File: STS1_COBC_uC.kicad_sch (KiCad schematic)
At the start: 42 parts, among them IC2 STWD100PYW83F, IC3 STM32F411RET6TR, J11 Conn_01x01_Male, J12 Conn_01x01_Male, J13 Conn_01x01_Male, J14 Conn_01x01_Male, J15 Conn_01x01_Male, J16 Conn_ARM_JTAG_SWD_10, J17 Conn_01x03_Male, J18 Conn_01x01_Male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

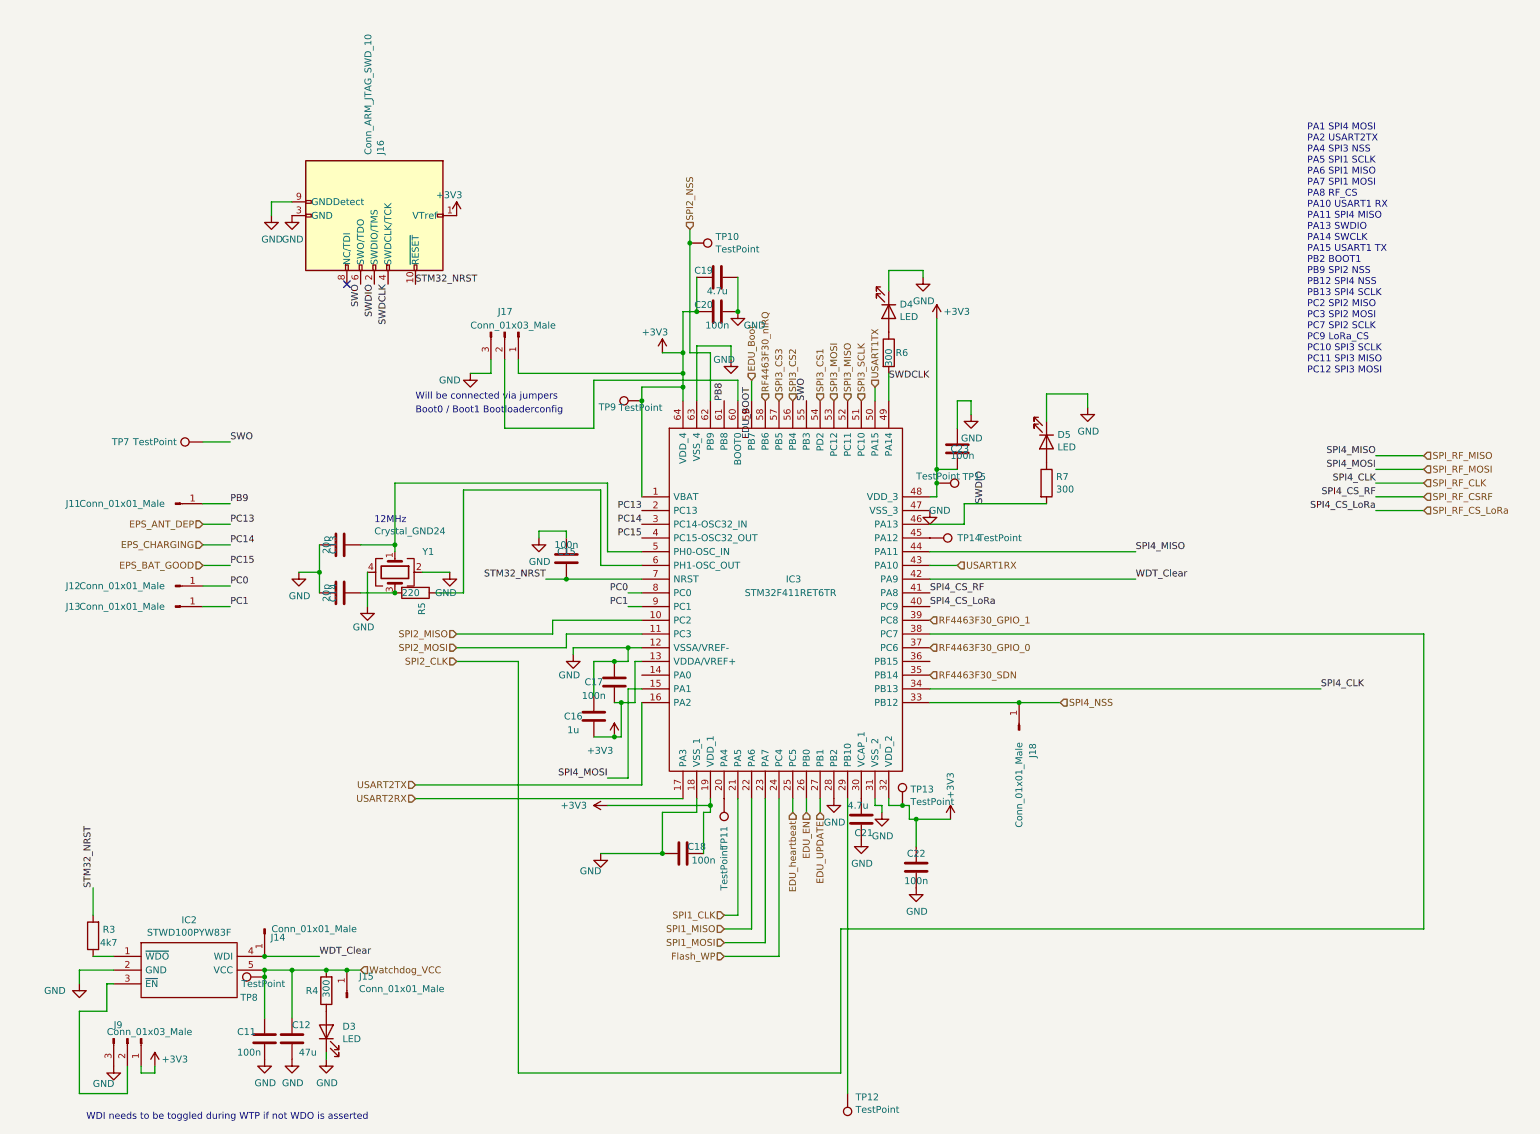
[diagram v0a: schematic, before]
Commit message: more work done
All parts besides RF added
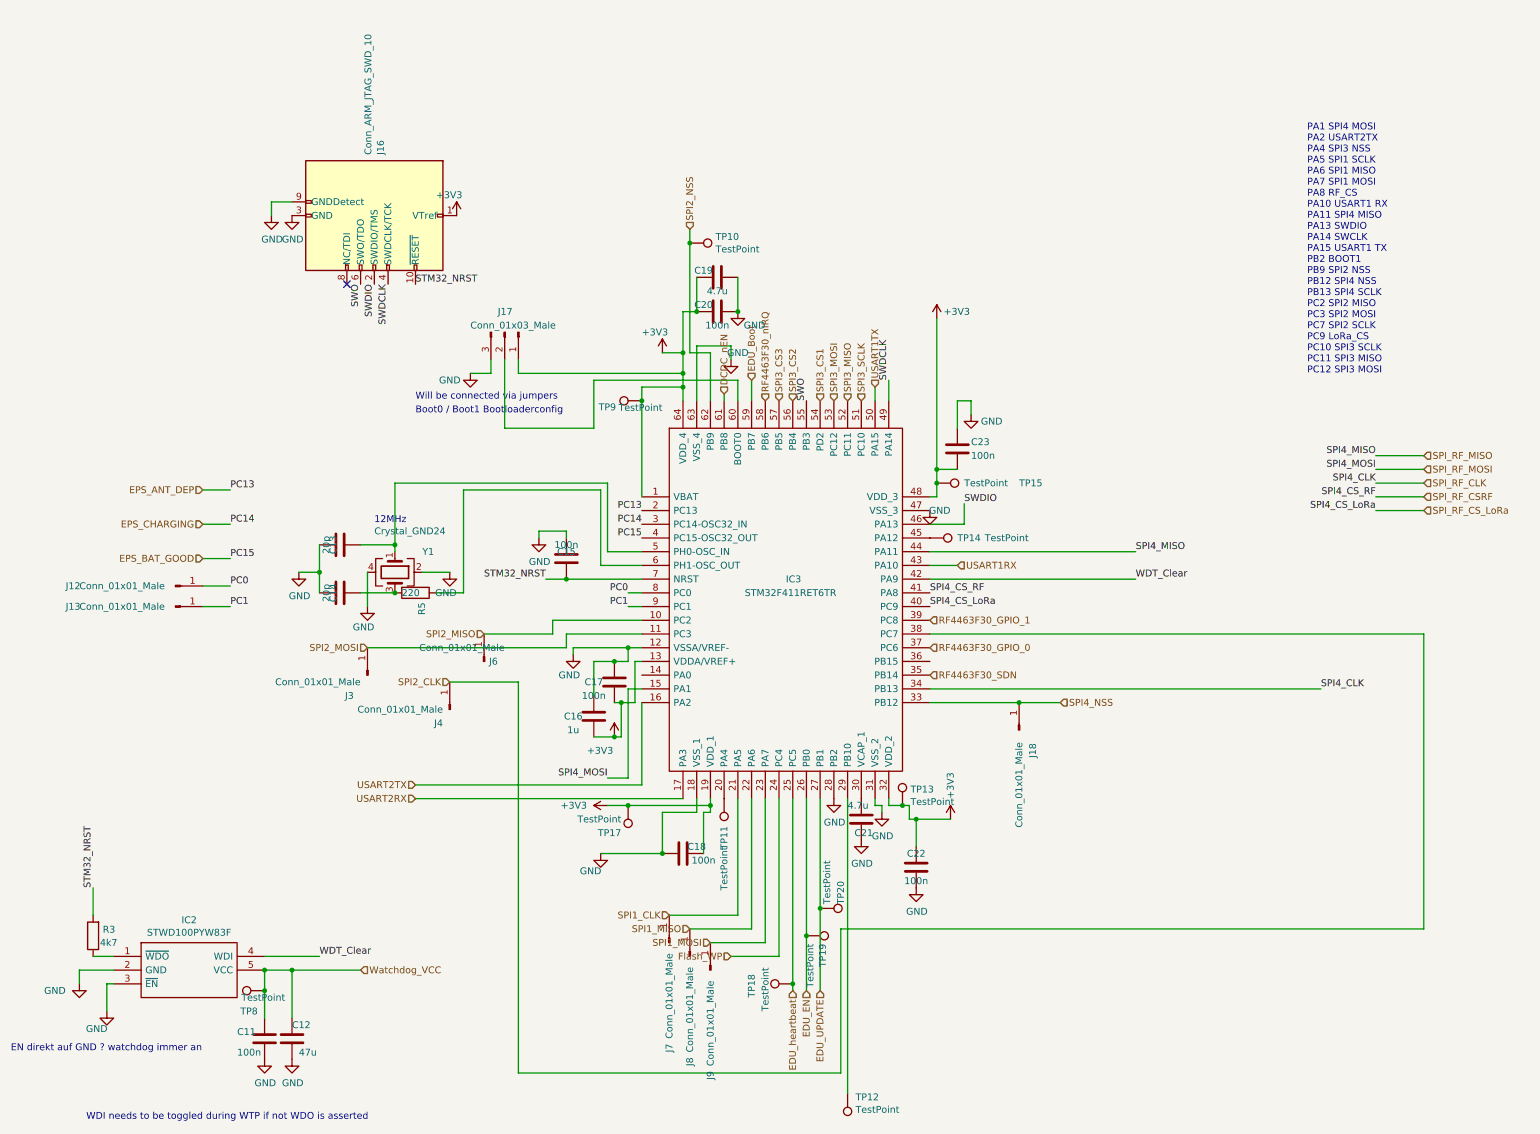
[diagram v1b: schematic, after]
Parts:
- removed D3, D4, D5: LED, LED_SMD:LED_0805_2012Metric, symbol Device:LED
- removed J11, J14, J15: Conn_01x01_Male, Connector_PinHeader_2.54mm:PinHeader_1x01_P2.54mm_Vertical, symbol Connector:Conn_01x01_Male
- removed J9: Conn_01x03_Male, STS1library:PinHeader_1x03_P2.54mm_Vertical_umdieEcke, symbol Connector:Conn_01x03_Male
- removed R4, R6, R7: 300, Resistor_SMD:R_0805_2012Metric, symbol Device:R
- removed TP7: TestPoint, STS1library:STS1_Testpoint, symbol Connector:TestPoint
- added J3, J4, J6, J7, J8, J9: Conn_01x01_Male, Connector_PinHeader_2.54mm:PinHeader_1x01_P2.54mm_Vertical, symbol Connector:Conn_01x01_Male
- added TP17, TP18, TP19, TP20: TestPoint, STS1library:STS1_Testpoint, symbol Connector:TestPoint
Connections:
- net +3V3: now also TP17.1
- net EDU_EN: now also TP19.1
- net EDU_UPDATE: now also TP20.1
- net EDU_heartbeat: now also TP18.1
- net GND: now also IC2.3 (~{EN})
- net SPI1_CLK: now also J7.1 (Pin_1)
- net SPI1_MISO: now also J8.1 (Pin_1)
- net SPI1_MOSI: now also J9.1 (Pin_1)
- net SPI2_CLK: now also J4.1 (Pin_1)
- net SPI2_MISO: now also J6.1 (Pin_1)
- net SPI2_MOSI: now also J3.1 (Pin_1)
- net PB8 renamed DCDC_nEN
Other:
- note added: "EN direkt auf GND ? watchdog immer an"
- moved on the sheet: TP8

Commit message: add RF part
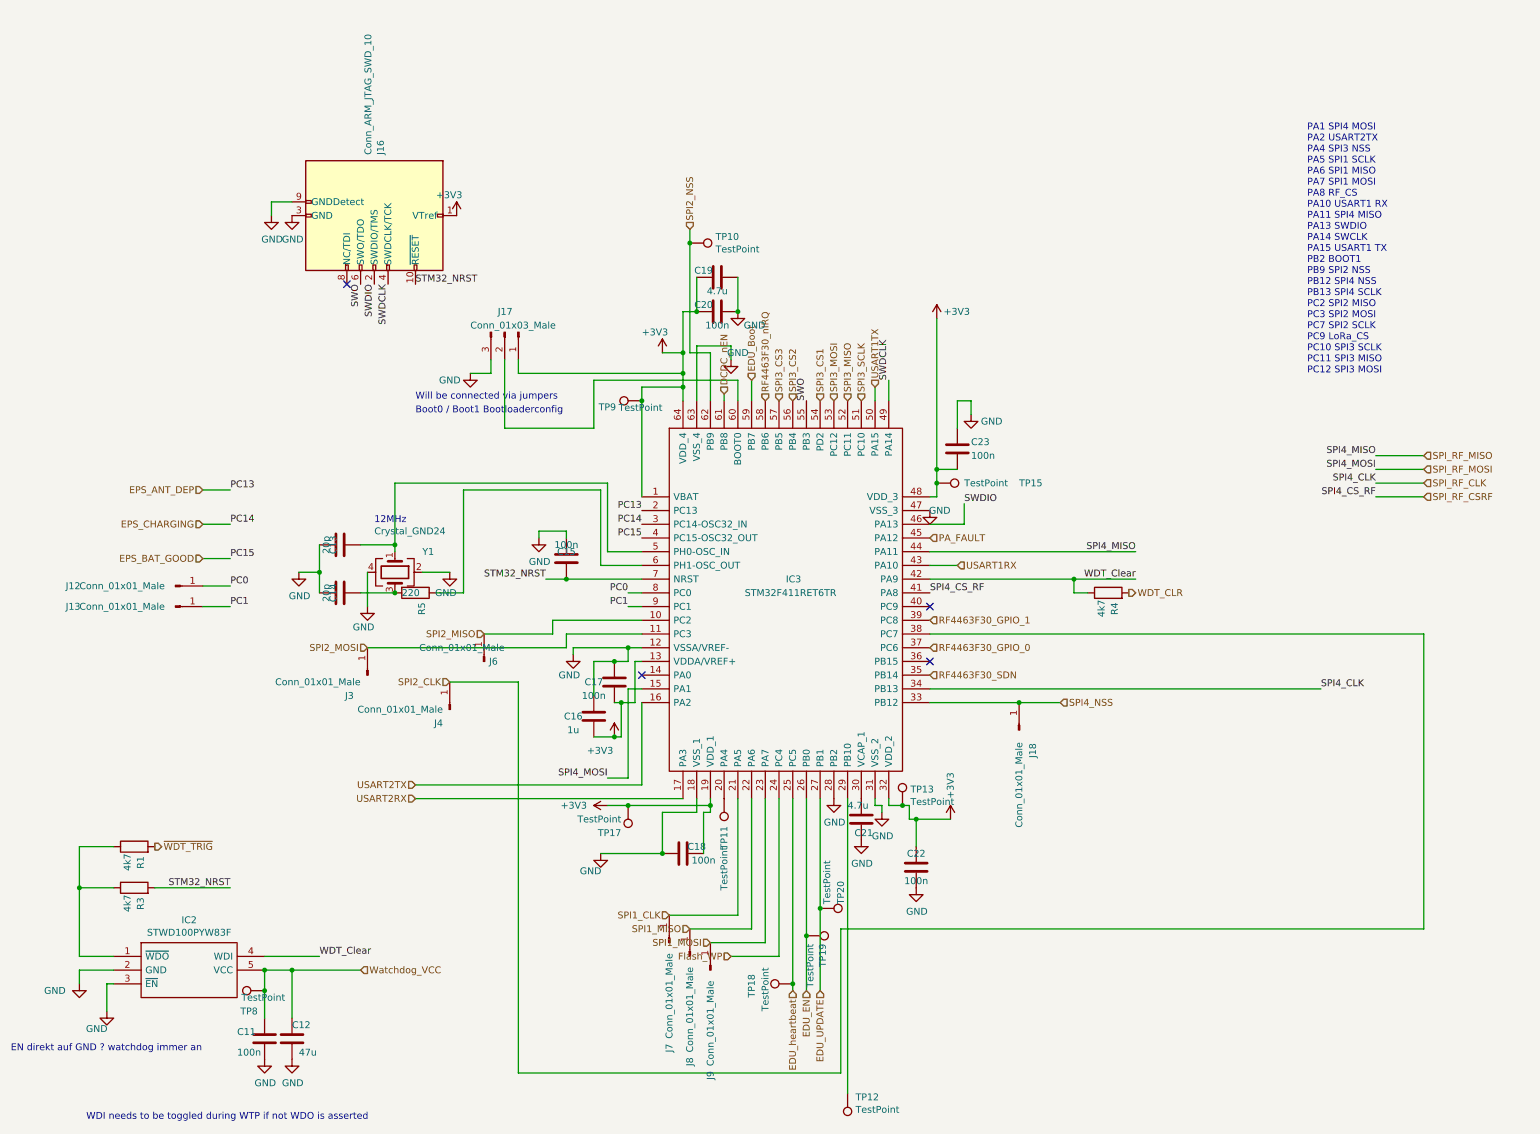
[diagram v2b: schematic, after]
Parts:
- removed TP14: TestPoint, STS1library:STS1_Testpoint, symbol Connector:TestPoint
- added R1, R4: 4k7, Resistor_SMD:R_0805_2012Metric, symbol Device:R
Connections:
- net WDT_Clear: now also R4.1
- net PA_FAULT: now reaches IC3.45 (PA12)
- net at IC2.1 (~{WDO}), R3.1: now also R1.1
- net SPI_RF_CS_LoRa: no longer names the net of IC3.40 (PC9)
- new net WDT_CLR: R4.2
- new net ~{WDT_TRIG}: R1.2
- no-connect marks 1 -> 4
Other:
- moved on the sheet: R3
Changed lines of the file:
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@@
   (junction (at 62.23 91.44) (diameter 0) (color 0 0 0 0)
   )
+  (junction (at 17.78 149.86) (diameter 0) (color 0 0 0 0)
+  )
   (junction (at 129.54 54.61) (diameter 0) (color 0 0 0 0)
   )
@@
   (junction (at 129.54 57.15) (diameter 0) (color 0 0 0 0)
   )
+  (junction (at 201.93 92.71) (diameter 0) (color 0 0 0 0)
+  )
   (junction (at 176.53 72.39) (diameter 0) (color 0 0 0 0)
   )
@@
   (junction (at 57.15 165.1) (diameter 0) (color 0 0 0 0)
   )
+  (no_connect (at 121.92 110.49))
+  (no_connect (at 175.26 107.95))
+  (no_connect (at 175.26 97.79))
   (no_connect (at 67.31 38.1))
+  (wire (pts (xy 17.78 149.86) (xy 24.13 149.86))
+    (stroke (width 0) (type default) (color 0 0 0 0))
+  )
   (wire (pts (xy 147.32 162.56) (xy 147.32 133.35))
     (stroke (width 0) (type default) (color 0 0 0 0))
@@
     (stroke (width 0) (type default) (color 0 0 0 0))
   )
-  (wire (pts (xy 266.7 80.01) (xy 257.81 80.01))
-    (stroke (width 0) (type default) (color 0 0 0 0))
-  )
   (wire (pts (xy 52.07 168.91) (xy 52.07 173.99))
     (stroke (width 0) (type default) (color 0 0 0 0))
@@
     (stroke (width 0) (type default) (color 0 0 0 0))
   )
-  (wire (pts (xy 24.13 162.56) (xy 20.32 162.56))
+  (wire (pts (xy 17.78 162.56) (xy 17.78 149.86))
     (stroke (width 0) (type default) (color 0 0 0 0))
   )
@@
     (stroke (width 0) (type default) (color 0 0 0 0))
   )
+  (wire (pts (xy 24.13 142.24) (xy 17.78 142.24))
+    (stroke (width 0) (type default) (color 0 0 0 0))
+  )
   (wire (pts (xy 181.61 82.55) (xy 181.61 78.74))
     (stroke (width 0) (type default) (color 0 0 0 0))
@@
     (stroke (width 0) (type default) (color 0 0 0 0))
   )
-  (wire (pts (xy 175.26 92.71) (xy 213.36 92.71))
+  (wire (pts (xy 175.26 92.71) (xy 201.93 92.71))
+    (stroke (width 0) (type default) (color 0 0 0 0))
+  )
+  (wire (pts (xy 201.93 92.71) (xy 213.36 92.71))
     (stroke (width 0) (type default) (color 0 0 0 0))
   )
@@
     (stroke (width 0) (type default) (color 0 0 0 0))
   )
+  (wire (pts (xy 201.93 95.25) (xy 201.93 92.71))
+    (stroke (width 0) (type default) (color 0 0 0 0))
+  )
   (wire (pts (xy 130.81 27.94) (xy 130.81 30.48))
     (stroke (width 0) (type default) (color 0 0 0 0))
@@
     (stroke (width 0) (type default) (color 0 0 0 0))
   )
+  (wire (pts (xy 17.78 142.24) (xy 17.78 149.86))
+    (stroke (width 0) (type default) (color 0 0 0 0))
+  )
   (wire (pts (xy 134.62 50.8) (xy 134.62 59.69))
     (stroke (width 0) (type default) (color 0 0 0 0))
@@
     (stroke (width 0) (type default) (color 0 0 0 0))
   )
-  (wire (pts (xy 20.32 149.86) (xy 20.32 154.94))
+  (wire (pts (xy 45.72 149.86) (xy 31.75 149.86))
     (stroke (width 0) (type default) (color 0 0 0 0))
   )
@@
     (stroke (width 0) (type default) (color 0 0 0 0))
   )
+  (wire (pts (xy 17.78 162.56) (xy 24.13 162.56))
+    (stroke (width 0) (type default) (color 0 0 0 0))
+  )
   (wire (pts (xy 149.86 167.64) (xy 149.86 168.91))
     (stroke (width 0) (type default) (color 0 0 0 0))
@@
   )
   (wire (pts (xy 71.12 91.44) (xy 71.12 97.79))
+    (stroke (width 0) (type default) (color 0 0 0 0))
+  )
+  (wire (pts (xy 204.47 95.25) (xy 201.93 95.25))
     (stroke (width 0) (type default) (color 0 0 0 0))
   )
@@
     (effects (font (size 1.27 1.27)) (justify right bottom))
   )
-  (label "SPI4_CS_LoRa" (at 257.81 80.01 180)
-    (effects (font (size 1.27 1.27)) (justify right bottom))
-  )
   (label "SPI4_CS_RF" (at 175.26 95.25 0)
     (effects (font (size 1.27 1.27)) (justify left bottom))
@@
     (effects (font (size 1.27 1.27)) (justify left bottom))
   )
-  (label "SPI4_CS_LoRa" (at 175.26 97.79 0)
-    (effects (font (size 1.27 1.27)) (justify left bottom))
-  )
   (label "PC1" (at 119.38 97.79 180)
     (effects (font (size 1.27 1.27)) (justify right bottom))
@@
     (effects (font (size 1.27 1.27)) (justify right bottom))
   )
-  (label "SPI4_MISO" (at 213.36 87.63 0)
-    (effects (font (size 1.27 1.27)) (justify left bottom))
+  (label "SPI4_MISO" (at 213.36 87.63 180)
+    (effects (font (size 1.27 1.27)) (justify right bottom))
   )
   (label "PC1" (at 45.72 97.79 0)
@@
     (effects (font (size 1.27 1.27)) (justify right bottom))
   )
-  (label "WDT_Clear" (at 213.36 92.71 0)
-    (effects (font (size 1.27 1.27)) (justify left bottom))
-  )
-  (label "STM32_NRST" (at 20.32 149.86 90)
-    (effects (font (size 1.27 1.27)) (justify left bottom))
-  )
-  (hierarchical_label "SPI_RF_CS_LoRa" (shape input) (at 266.7 80.01 0)
+  (label "WDT_Clear" (at 213.36 92.71 180)
+    (effects (font (size 1.27 1.27)) (justify right bottom))
+  )
+  (label "STM32_NRST" (at 45.72 149.86 180)
+    (effects (font (size 1.27 1.27)) (justify right bottom))
+  )
+  (hierarchical_label "~{WDT_TRIG}" (shape output) (at 31.75 142.24 0)
     (effects (font (size 1.27 1.27)) (justify left))
   )
@@
     (effects (font (size 1.27 1.27)) (justify left))
   )
+  (hierarchical_label "PA_FAULT" (shape input) (at 175.26 85.09 0)
+    (effects (font (size 1.27 1.27)) (justify left))
+  )
   (hierarchical_label "USART1RX" (shape input) (at 180.34 90.17 0)
     (effects (font (size 1.27 1.27)) (justify left))
@@
   )
   (hierarchical_label "RF4463F30_nIRQ" (shape input) (at 144.78 59.69 90)
+    (effects (font (size 1.27 1.27)) (justify left))
+  )
+  (hierarchical_label "WDT_CLR" (shape output) (at 212.09 95.25 0)
     (effects (font (size 1.27 1.27)) (justify left))
   )
@@
     (pin "1")
   )
-  (symbol (lib_id "Device:R") (at 20.32 158.75 180) (unit 1)
-    (in_bom yes) (on_board yes)
-    (property "Reference" "R3" (id 0) (at 22.098 157.5816 0)
+  (symbol (lib_id "Device:R") (at 27.94 149.86 90) (unit 1)
+    (in_bom yes) (on_board yes)
+    (property "Reference" "R3" (id 0) (at 29.1084 151.638 0)
       (effects (font (size 1.27 1.27)) (justify right))
     )
-    (property "Value" "4k7" (id 1) (at 21.59 160.02 0)
+    (property "Value" "4k7" (id 1) (at 26.67 151.13 0)
       (effects (font (size 1.27 1.27)) (justify right))
     )
-    (property "Footprint" "Resistor_SMD:R_0805_2012Metric" (id 2) (at 22.098 158.75 90)
-      (effects (font (size 1.27 1.27)) hide)
-    )
-    (property "Datasheet" "~" (id 3) (at 20.32 158.75 0)
+    (property "Footprint" "Resistor_SMD:R_0805_2012Metric" (id 2) (at 27.94 151.638 90)
+      (effects (font (size 1.27 1.27)) hide)
+    )
+    (property "Datasheet" "~" (id 3) (at 27.94 149.86 0)
       (effects (font (size 1.27 1.27)) hide)
     )
@@
     (pin "1")
   )
-  (symbol (lib_id "Connector:TestPoint") (at 175.26 85.09 270) (unit 1)
-    (in_bom yes) (on_board yes)
-    (property "Reference" "TP14" (id 0) (at 180.34 85.09 90)
-      (effects (font (size 1.27 1.27)) (justify left))
-    )
-    (property "Value" "TestPoint" (id 1) (at 185.42 85.09 90)
-      (effects (font (size 1.27 1.27)) (justify left))
-    )
-    (property "Footprint" "STS1library:STS1_Testpoint" (id 2) (at 175.26 90.17 0)
-      (effects (font (size 1.27 1.27)) hide)
-    )
-    (property "Datasheet" "~" (id 3) (at 175.26 90.17 0)
-      (effects (font (size 1.27 1.27)) hide)
-    )
-    (pin "1")
-  )
   (symbol (lib_id "Device:Crystal_GND24") (at 76.2 91.44 270) (unit 1)
     (in_bom yes) (on_board yes)
@@
     (pin "1")
   )
+  (symbol (lib_id "Device:R") (at 27.94 142.24 90) (unit 1)
+    (in_bom yes) (on_board yes)
+    (property "Reference" "R1" (id 0) (at 29.1084 144.018 0)
+      (effects (font (size 1.27 1.27)) (justify right))
+    )
+    (property "Value" "4k7" (id 1) (at 26.67 143.51 0)
+      (effects (font (size 1.27 1.27)) (justify right))
+    )
+    (property "Footprint" "Resistor_SMD:R_0805_2012Metric" (id 2) (at 27.94 144.018 90)
+      (effects (font (size 1.27 1.27)) hide)
+    )
+    (property "Datasheet" "~" (id 3) (at 27.94 142.24 0)
+      (effects (font (size 1.27 1.27)) hide)
+    )
+    (pin "1")
+    (pin "2")
+  )
   (symbol (lib_id "Connector:Conn_01x01_Male") (at 130.81 162.56 90) (unit 1)
     (in_bom yes) (on_board yes)
@@
     (pin "1")
   )
+  (symbol (lib_id "Device:R") (at 208.28 95.25 90) (unit 1)
+    (in_bom yes) (on_board yes)
+    (property "Reference" "R4" (id 0) (at 209.4484 97.028 0)
+      (effects (font (size 1.27 1.27)) (justify right))
+    )
+    (property "Value" "4k7" (id 1) (at 207.01 96.52 0)
+      (effects (font (size 1.27 1.27)) (justify right))
+    )
+    (property "Footprint" "Resistor_SMD:R_0805_2012Metric" (id 2) (at 208.28 97.028 90)
+      (effects (font (size 1.27 1.27)) hide)
+    )
+    (property "Datasheet" "~" (id 3) (at 208.28 95.25 0)
+      (effects (font (size 1.27 1.27)) hide)
+    )
+    (pin "1")
+    (pin "2")
+  )
   (symbol (lib_id "Connector:TestPoint") (at 152.4 158.75 270) (unit 1)
